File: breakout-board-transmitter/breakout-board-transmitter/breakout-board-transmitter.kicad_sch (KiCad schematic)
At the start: 19 parts, among them U1 CC1100-RTR1, Y1 Crystal

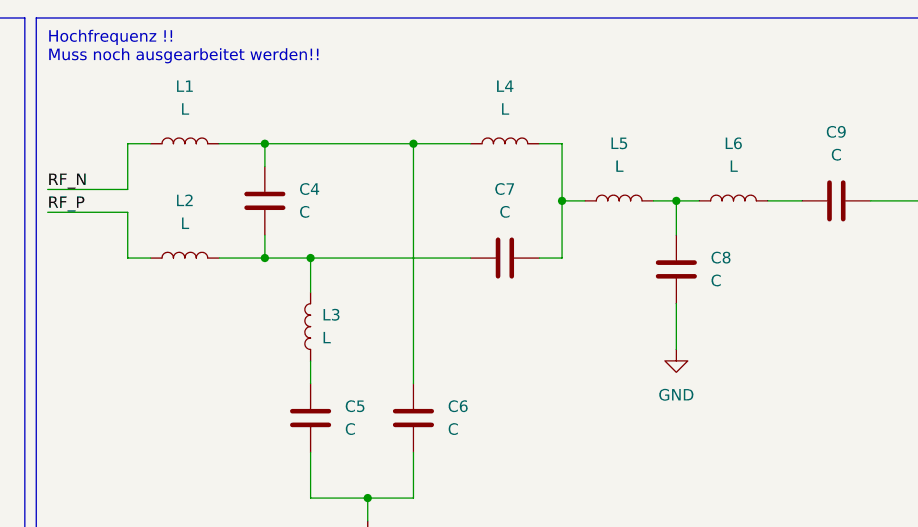
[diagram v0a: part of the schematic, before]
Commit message: KiCad 7.0
Updated to KiCad 7.0 file format
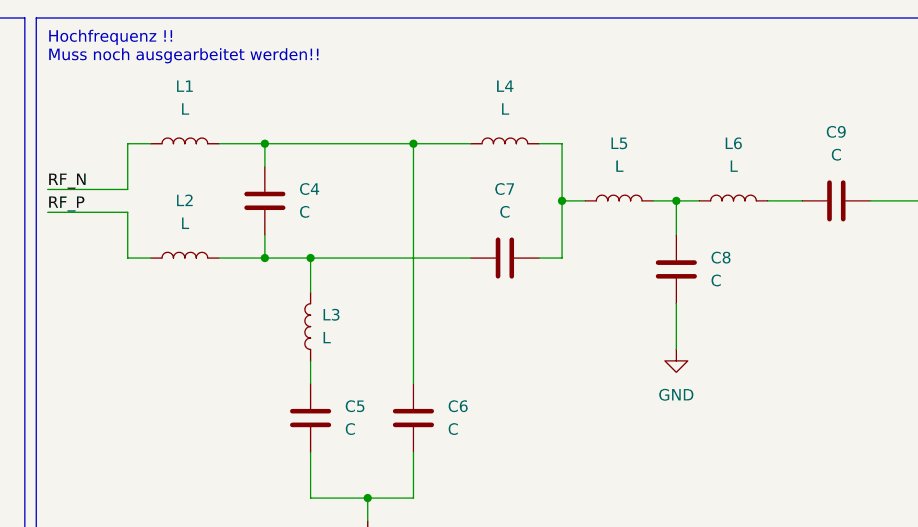
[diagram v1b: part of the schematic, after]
